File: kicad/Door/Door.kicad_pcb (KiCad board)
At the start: 2 copper layers, 49.5 x 50.5 mm, 18 parts, among them Q1 Q_NMOS_GDS, Q2 Q_PMOS_GSD, SW1 SW_Push, SW2 USB/BAT, SW3 RST_BTN, U1 NODEMCU v3

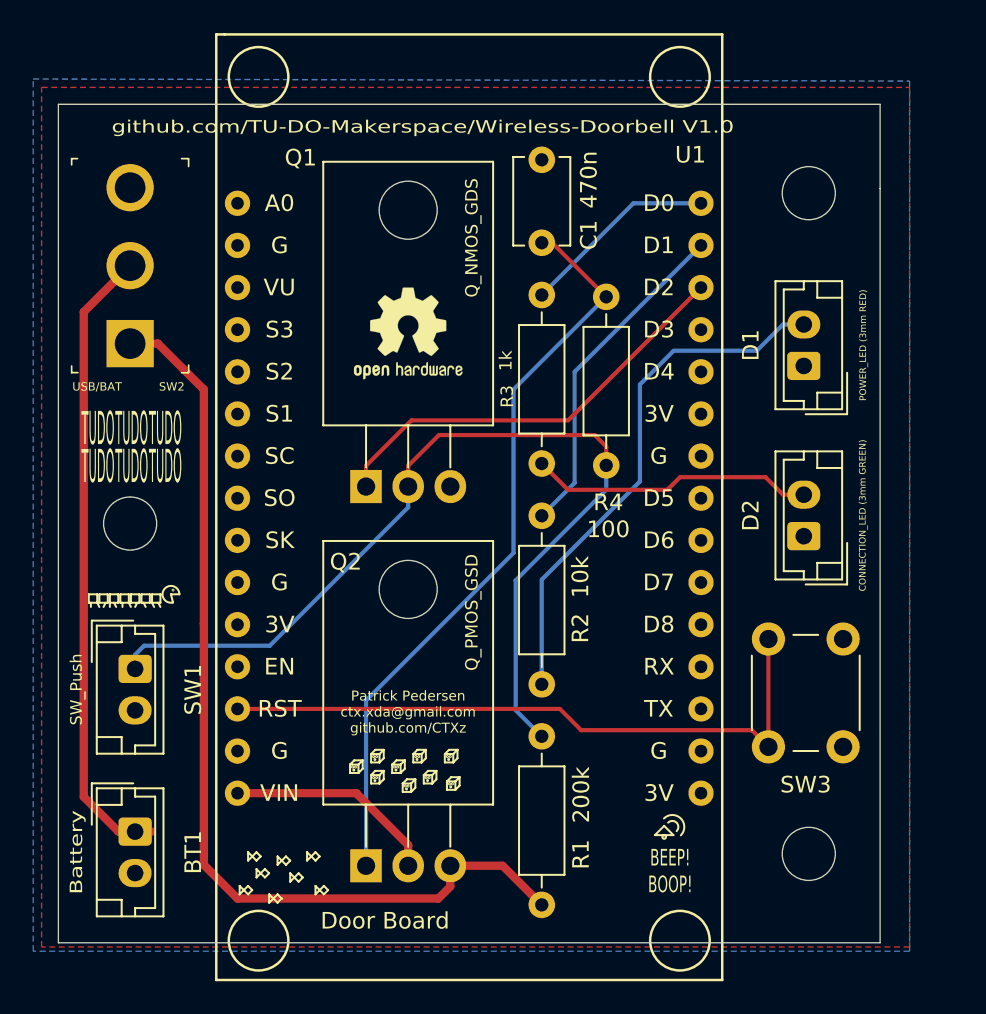
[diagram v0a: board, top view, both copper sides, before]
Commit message: Git: Ignore kicad backups and cache files
Signed-off-by: CTXz <ctx.xda@gmail.com>
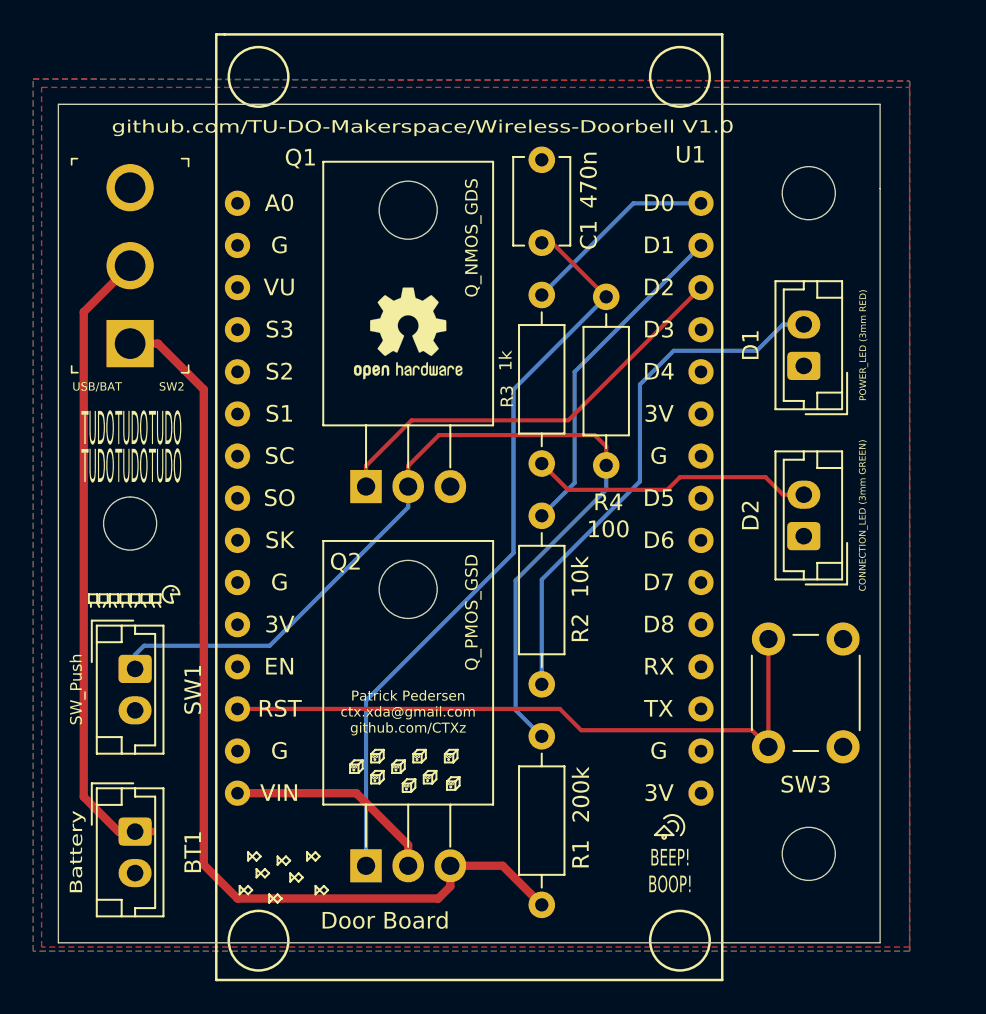
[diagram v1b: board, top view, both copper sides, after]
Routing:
- added copper zone on B.Cu, net GND
- removed copper zone on B.Cu, net (none)
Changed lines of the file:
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@@
   (segment (start 84.344001 127.397001) (end 83.058 126.111) (width 0.25) (layer "F.Cu") (net 30))
   (segment (start 95.631 128.397) (end 95.631 121.897) (width 0.25) (layer "F.Cu") (net 30))
+  (zone (net 1) (net_name "GND") (layers F&B.Cu) (hatch edge 0.508)
+    (connect_pads (clearance 0.508))
+    (min_thickness 0.254) (filled_areas_thickness no)
+    (fill yes (thermal_gap 0.508) (thermal_bridge_width 0.508))
+    (polygon
+      (pts
+        (xy 104.14 88.265)
+        (xy 104.14 140.716)
+        (xy 51.308 140.716)
+        (xy 51.308 88.138)
+      )
+    )
+  )
   (zone (net 1) (net_name "GND") (layer "F.Cu") (hatch edge 0.508)
     (connect_pads (clearance 0.508))
-    (min_thickness 0.254)
+    (min_thickness 0.254) (filled_areas_thickness no)
     (fill yes (thermal_gap 0.508) (thermal_bridge_width 0.508))
     (polygon
@@
       )
     )
-  )
-  (zone (net 0) (net_name "") (layer "B.Cu") (hatch edge 0.508)
-    (connect_pads (clearance 0.508))
-    (min_thickness 0.254)
-    (fill yes (thermal_gap 0.508) (thermal_bridge_width 0.508))
-    (polygon
-      (pts
-        (xy 104.14 88.265)
-        (xy 104.14 140.716)
-        (xy 51.308 140.716)
-        (xy 51.308 88.138)
-      )
-    )

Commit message: Kicad: Door: Fixed bottom plane not connected to GND net + Changed USB/BAT to BAT CON/DISCON on SW2 + Added labels for SW2 + Moved github link and board name to backside
Signed-off-by: CTXz <ctx.xda@gmail.com>
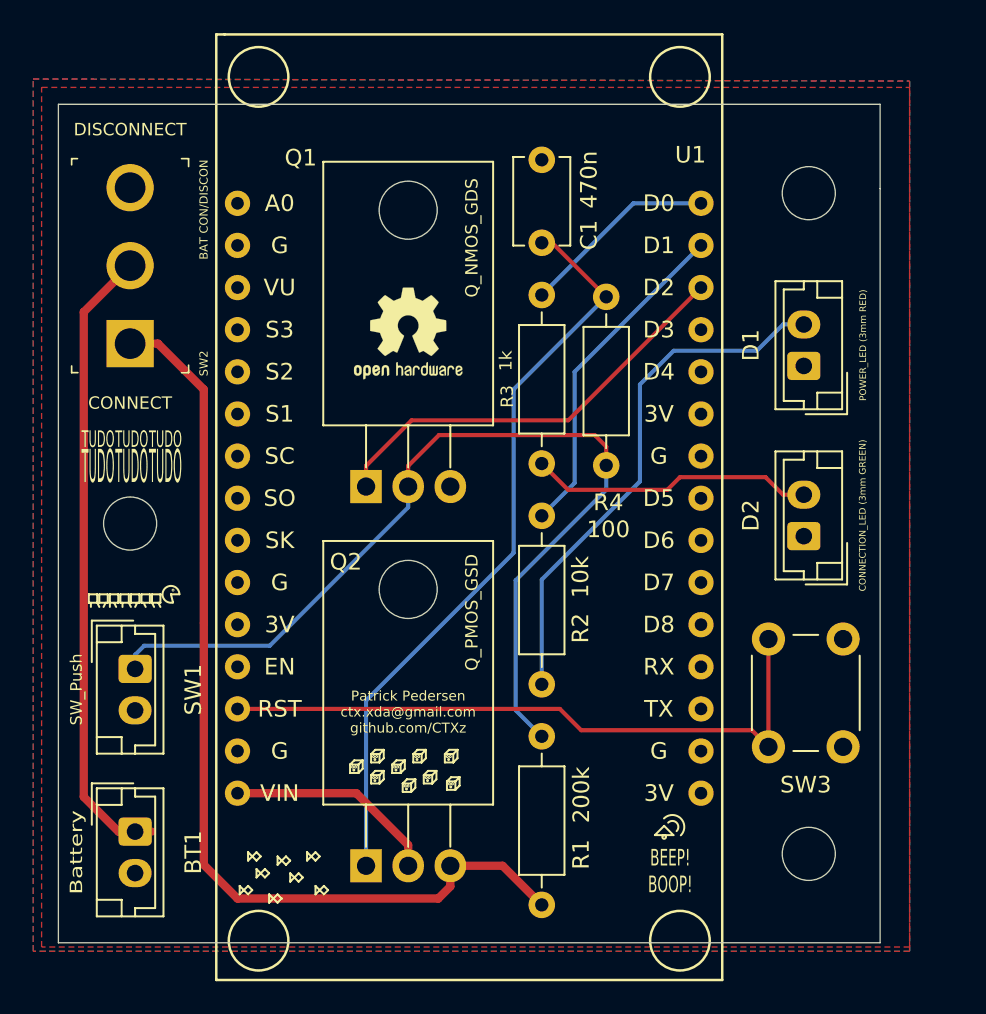
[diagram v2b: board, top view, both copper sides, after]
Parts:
- SW2: value USB/BAT -> BAT CON/DISCON
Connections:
- U1 pad 1: Net-(U1-Pad1) -> unconnected-(U1-Pad1)
- U1 pad 11: (no net) -> unconnected-(U1-Pad11)
- U1 pad 12: Net-(U1-Pad12) -> unconnected-(U1-Pad12)
- U1 pad 16: (no net) -> unconnected-(U1-Pad16)
- U1 pad 18: Net-(U1-Pad18) -> unconnected-(U1-Pad18)
- U1 pad 19: Net-(U1-Pad19) -> unconnected-(U1-Pad19)
- U1 pad 2: Net-(U1-Pad2) -> unconnected-(U1-Pad2)
- U1 pad 20: Net-(U1-Pad20) -> unconnected-(U1-Pad20)
- U1 pad 21: Net-(U1-Pad21) -> unconnected-(U1-Pad21)
- U1 pad 22: Net-(U1-Pad22) -> unconnected-(U1-Pad22)
- U1 pad 23: Net-(U1-Pad23) -> unconnected-(U1-Pad23)
- U1 pad 25: (no net) -> unconnected-(U1-Pad25)
- U1 pad 26: Net-(U1-Pad26) -> unconnected-(U1-Pad26)
- U1 pad 3: Net-(U1-Pad3) -> unconnected-(U1-Pad3)
- U1 pad 4: Net-(U1-Pad4) -> unconnected-(U1-Pad4)
- U1 pad 5: Net-(U1-Pad5) -> unconnected-(U1-Pad5)
- U1 pad 6: Net-(U1-Pad6) -> unconnected-(U1-Pad6)
- U1 pad 7: Net-(U1-Pad7) -> unconnected-(U1-Pad7)
- U1 pad 8: Net-(U1-Pad8) -> unconnected-(U1-Pad8)
- U1 pad 9: Net-(U1-Pad9) -> unconnected-(U1-Pad9)
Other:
- board text added: "CONNECT"
- board text added: "DISCONNECT"
- board text added: "github.com/TU-DO-Makerspace/Wireless-Doorbell V1.01"
- board text removed: "github.com/TU-DO-Makerspace/Wireless-Doorbell V1.0"
